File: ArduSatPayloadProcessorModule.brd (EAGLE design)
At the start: 95.5 x 90.3 mm, 339 parts, among them IC1 ATMEGA328P QFN32, IC10 ATMEGA328P QFN32, IC11 ATMEGA328P QFN32, IC12 ATMEGA328P QFN32, IC13 ATMEGA328P QFN32, IC14 ATMEGA328P QFN32, IC15 ATMEGA328P QFN32, IC16 ATMEGA328P QFN32, IC17 TXB0104, IC18 TMP102, IC19 TMP102, IC2 ATMEGA328P QFN32, IC20 ATMEGA2561-16MU, IC21 MAX4372F, IC22 MAX4372F, IC23 MUX-74HC4067-QFNSMT, IC24 MUX-74HC4067-QFNSMT, IC3 ATMEGA328P QFN32, IC4 ATMEGA328P QFN32, IC5 ATMEGA328P QFN32, IC6 ATMEGA328P QFN32, IC7 ATMEGA328P QFN32, IC8 ATMEGA328P QFN32, IC9 ATMEGA328P QFN32, P1 microSD, Q1 RJU003N03 N-MOSFET, Q10 RJU003N03 N-MOSFET, Q11 RJU003N03 N-MOSFET, Q12 RJU003N03 N-MOSFET, Q13 RJU003N03 N-MOSFET, Q14 RJU003N03 N-MOSFET, Q15 RJU003N03 N-MOSFET, Q16 RJU003N03 N-MOSFET, Q17 RJU003N03 N-MOSFET, Q18 RJU003N03 N-MOSFET, Q19 RJU003N03 N-MOSFET, Q2 RJU003N03 N-MOSFET, Q20 RJU003N03 N-MOSFET, Q21 RJU003N03 N-MOSFET, Q22 RJU003N03 N-MOSFET, Q23 RJU003N03 N-MOSFET, Q24 RJU003N03 N-MOSFET, Q25 RJU003N03 N-MOSFET, Q26 RJU003N03 N-MOSFET, Q27 RJU003N03 N-MOSFET, Q28 RJU003N03 N-MOSFET, Q29 RJU003N03 N-MOSFET, Q3 RJU003N03 N-MOSFET, Q30 RJU003N03 N-MOSFET, Q31 RJU003N03 N-MOSFET, Q32 RJU003N03 N-MOSFET, Q33 RJU003N03 N-MOSFET, Q34 RJU003N03 N-MOSFET, Q35 RJU003N03 N-MOSFET, Q36 RJU003N03 N-MOSFET, Q37 RJU003N03 N-MOSFET, Q38 RJU003N03 N-MOSFET, Q39 RJU003N03 N-MOSFET, Q4 RJU003N03 N-MOSFET, Q40 RJU003N03 N-MOSFET, Q41 RJU003N03 N-MOSFET, Q42 RJU003N03 N-MOSFET, Q43 RJU003N03 N-MOSFET, Q44 RJU003N03 N-MOSFET, Q45 RJU003N03 N-MOSFET, Q46 RJU003N03 N-MOSFET, Q5 RJU003N03 N-MOSFET, Q6 RJU003N03 N-MOSFET, Q7 RJU003N03 N-MOSFET, Q8 RJU003N03 N-MOSFET, Q9 RJU003N03 N-MOSFET, SW1 ADG801 SOT23-6, SW10 ADG801 SOT23-6, SW11 ADG801 SOT23-6, SW12 ADG801 SOT23-6, SW13 ADG801 SOT23-6, SW14 ADG801 SOT23-6, SW15 ADG801 SOT23-6, SW16 ADG801 SOT23-6, SW17 RESET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

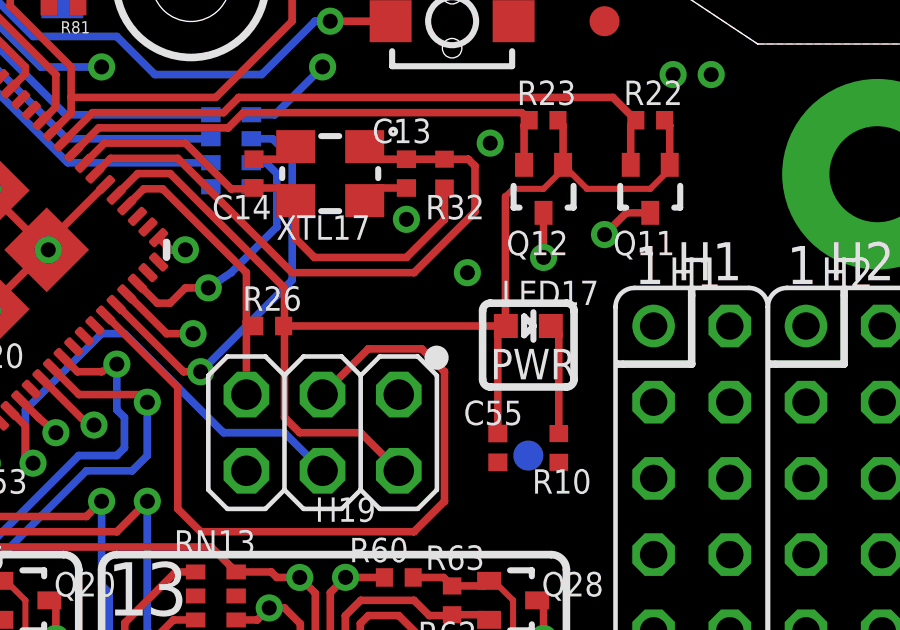
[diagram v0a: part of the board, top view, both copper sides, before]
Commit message: Switched PWR LED to 0402
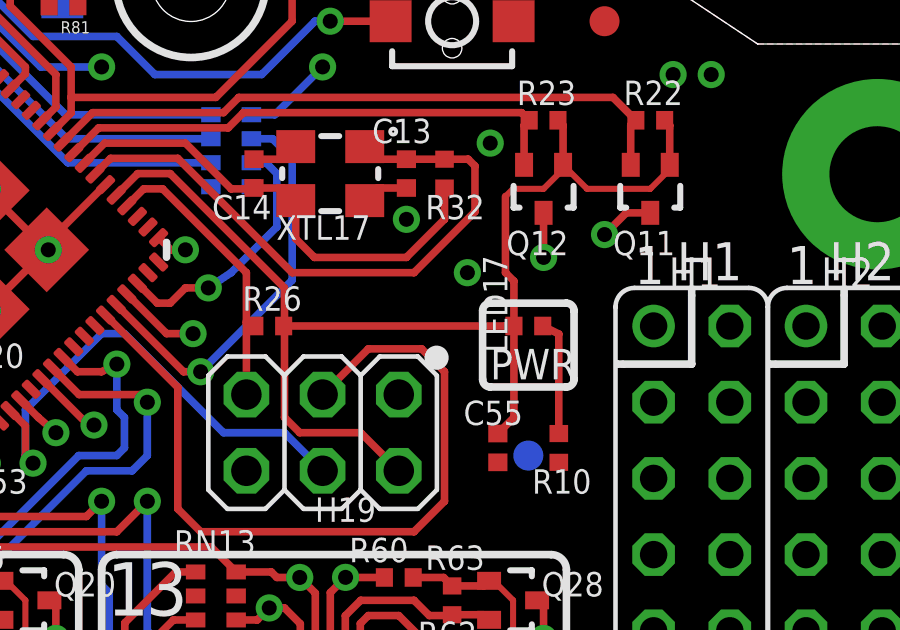
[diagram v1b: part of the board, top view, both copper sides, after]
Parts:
- LED17: device freetronics:LED-0603 -> freetronics-jon:LED-0402
- turned LED17 to 0 degrees
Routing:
- net 5V: track 619.0 -> 619.8 mm
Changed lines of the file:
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@@
 <attribute name="VALUE" x="80.9752" y="71.12" size="0.4064" layer="27" font="vector" rot="R90"/>
 </element>
-<element name="LED17" library="freetronics" package="LED-0603" value="BLUE 0603" x="78.994" y="76.2" smashed="yes" rot="R270">
-<attribute name="NAME" x="78.105" y="76.8985" size="0.8128" layer="25"/>
-<attribute name="VALUE" x="77.978" y="75.1205" size="0.4064" layer="27"/>
+<element name="LED17" library="freetronics-jon" package="LED-0402" value="BLUE 0603" x="78.994" y="76.2" smashed="yes">
+<attribute name="NAME" x="78.2955" y="75.311" size="0.8128" layer="25" rot="R90"/>
+<attribute name="VALUE" x="80.0735" y="75.184" size="0.4064" layer="27" rot="R90"/>
 </element>
 <element name="R4" library="freetronics-jon" package="0402" value="10K 0402" x="27.051" y="7.112" smashed="yes" rot="R270">
@@
 <contactref element="R10" pad="2"/>
 <contactref element="LED17" pad="C"/>
-<wire x1="79.744" y1="76.2" x2="80.01" y2="75.934" width="0.254" layer="1"/>
+<wire x1="79.474" y1="76.2" x2="80.01" y2="75.934" width="0.254" layer="1"/>
 <wire x1="80.01" y1="75.934" x2="80.01" y2="72.616" width="0.254" layer="1"/>
 </signal>
@@
 <wire x1="79.502" y1="80.772" x2="78.486" y2="80.772" width="0.2032" layer="1"/>
 <wire x1="78.486" y1="80.772" x2="78.232" y2="80.518" width="0.2032" layer="1"/>
-<wire x1="78.244" y1="76.2" x2="77.978" y2="75.934" width="0.254" layer="1"/>
-<wire x1="77.978" y1="75.934" x2="77.978" y2="72.616" width="0.254" layer="1"/>
-<wire x1="78.244" y1="76.2" x2="70.838" y2="76.2" width="0.254" layer="1"/>
+<wire x1="78.514" y1="76.2" x2="70.838" y2="76.2" width="0.254" layer="1"/>
 <wire x1="70.866" y1="73.152" x2="70.866" y2="76.101" width="0.254" layer="1"/>
 <wire x1="70.866" y1="76.101" x2="70.866" y2="76.172" width="0.254" layer="1"/>
 <wire x1="70.866" y1="76.172" x2="70.838" y2="76.2" width="0.254" layer="1"/>
-<wire x1="78.232" y1="80.518" x2="78.232" y2="76.212" width="0.254" layer="1"/>
-<wire x1="78.232" y1="76.212" x2="78.244" y2="76.2" width="0.254" layer="1"/>
+<wire x1="78.232" y1="76.212" x2="78.514" y2="76.2" width="0.254" layer="1"/>
 <wire x1="77.343" y1="42.037" x2="77.216" y2="41.91" width="0.6096" layer="1"/>
 <wire x1="77.216" y1="41.91" x2="74.168" y2="41.91" width="0.6096" layer="1"/>
@@
 <wire x1="22.38" y1="83.058" x2="22.38" y2="81.816" width="0.3048" layer="16"/>
 <wire x1="22.38" y1="81.816" x2="22.352" y2="81.788" width="0.3048" layer="16"/>
+<wire x1="77.978" y1="72.616" x2="78.514" y2="73.152" width="0.254" layer="1"/>
+<wire x1="78.514" y1="73.152" x2="78.514" y2="76.2" width="0.254" layer="1"/>
+<wire x1="78.232" y1="80.518" x2="78.232" y2="77.978" width="0.254" layer="1"/>
+<wire x1="78.232" y1="77.978" x2="78.514" y2="77.696" width="0.254" layer="1"/>
+<wire x1="78.514" y1="77.696" x2="78.514" y2="76.2" width="0.254" layer="1"/>
 </signal>
 <signal name="VCC_SYS">

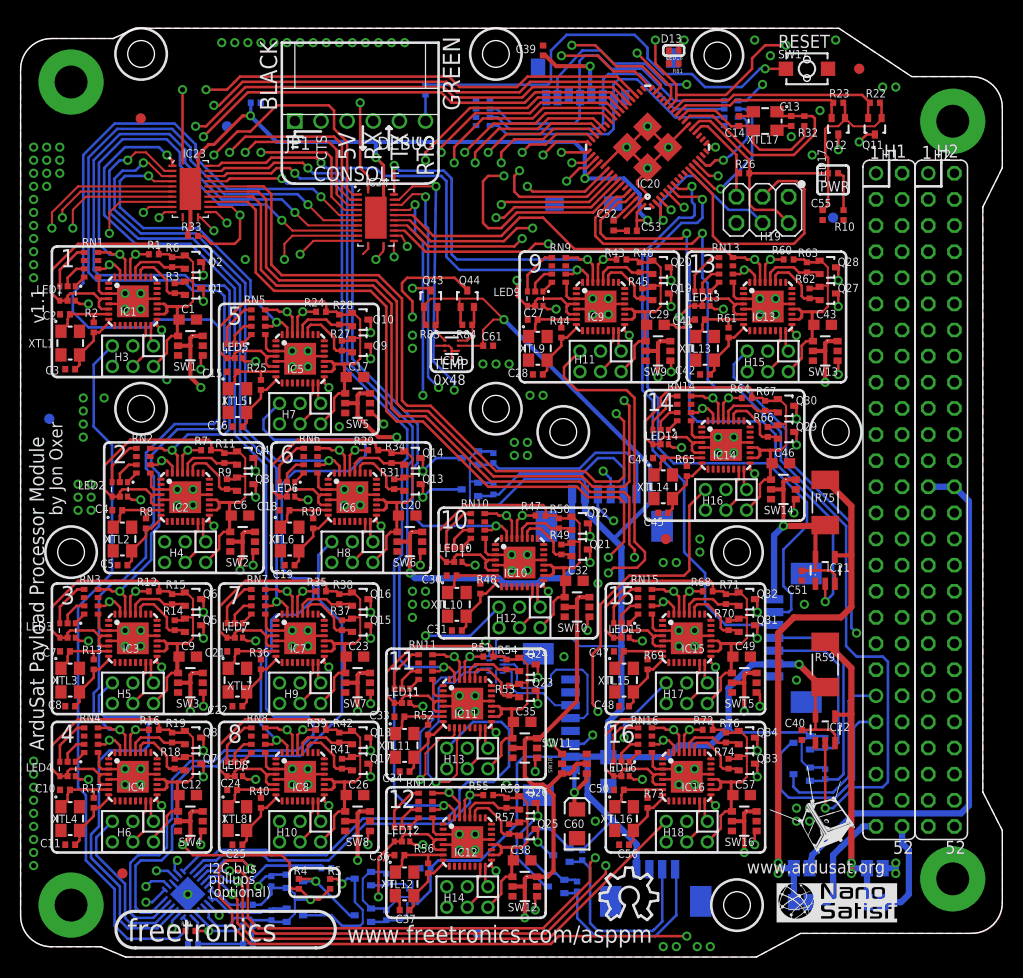
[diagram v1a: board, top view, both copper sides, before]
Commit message: Release 1.2: power jumpers on TMP102s; clearances
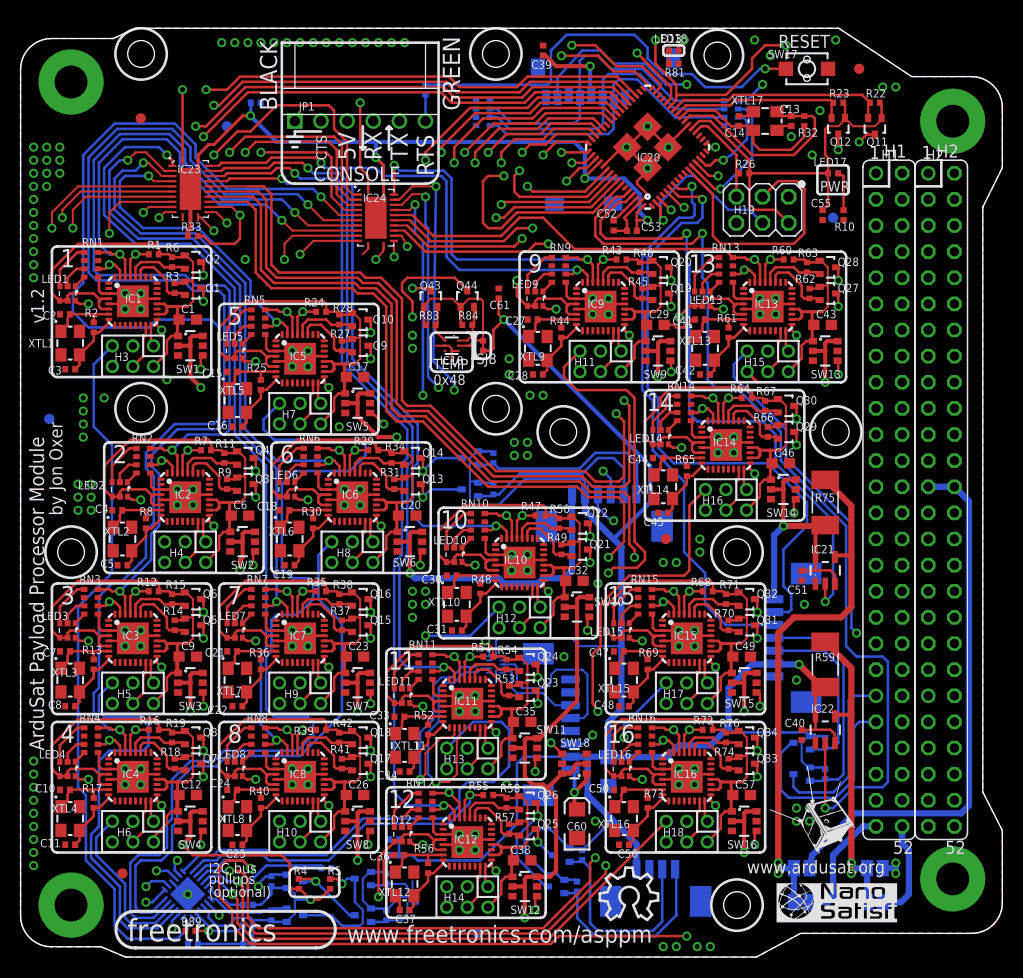
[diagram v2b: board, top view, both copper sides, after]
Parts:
- added SJ8, SJ9: SJC0402, freetronics-jon:0402SJC
- C59, C60: device freetronics:EIA3216 -> freetronics-jon:EIA3216
- LED17: value BLUE 0603 -> BLUE 0402
- P1: device freetronics-master-v1:MICRO-SD-SOCKET-PP -> freetronics-master-v1.1:MICRO-SD-SOCKET-PP
- moved C61 5.18 mm to (46.5, 64.5), turned to 90 degrees
- moved C62 4.13 mm to (36.3, 11.4)
- renumbered U$26 to IC25
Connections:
- new net N$10010: IC18.5, Q43.1, Q44.1, R83.2, R84.2, SJ8.2
- new net N$10011: IC19.4, IC19.5, Q45.1, Q46.1, R85.2, R86.2, SJ9.2
- net 3.3V: now also SJ8.1, SJ9.1; no longer IC18.5, IC19.4, IC19.5, Q43.1, Q44.1, Q45.1, Q46.1, R83.2, R84.2, R85.2, R86.2
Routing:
- net 3.3V: track 280.5 -> 252.1 mm
- net N$10010: track 0.00 -> 17.0 mm
- net N$10011: track 0.00 -> 13.4 mm
- net GND: track 273.5 -> 280.2 mm, vias 166 -> 165
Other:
- board text added: "IC25"
- board text added: "v1.2"
- board text removed: "v1.1"
